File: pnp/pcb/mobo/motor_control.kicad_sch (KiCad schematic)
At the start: 0 parts

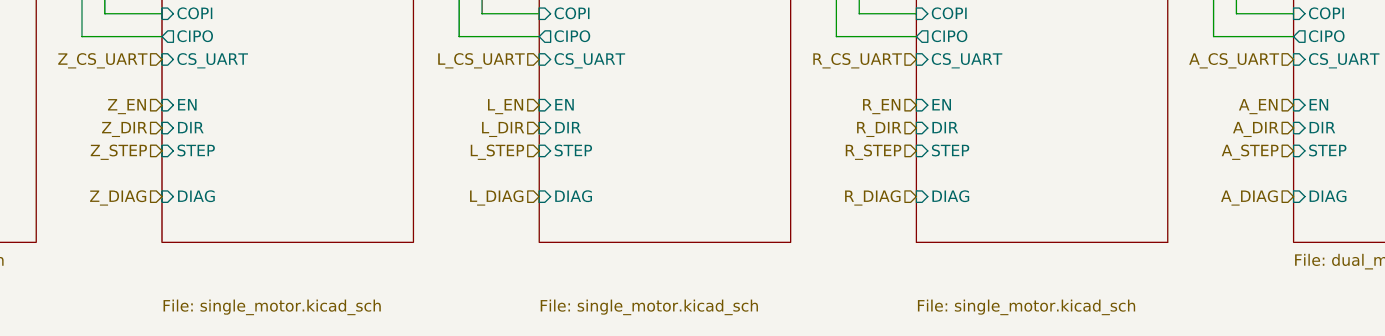
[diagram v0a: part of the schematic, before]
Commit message: Mobo V4A Redesign
Some EMC improvements to schematics.
Reassigned MCU Pins for HW-PWM support.
Changes are still marked with text in the schematics.
Complete PCB Layout reworked
Status: Needs to be verified, and cleaned up a little, but DRC is running green.
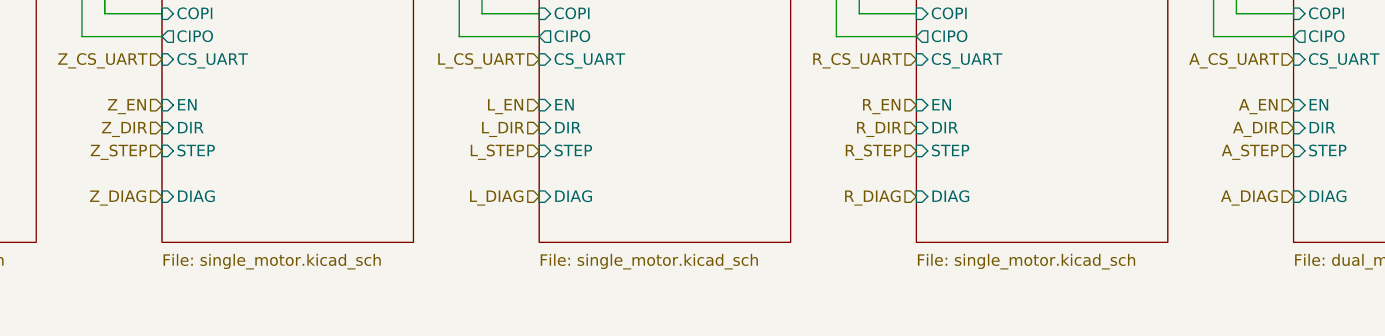
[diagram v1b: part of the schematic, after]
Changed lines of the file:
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@@
   (title_block
     (title "LumenPnP Motherboard")
-    (date "2022-03-29")
-    (rev "003")
+    (date "2022-09-09")
+    (rev "004A")
     (company "Opulo")
+    (comment 1 "Reengineered by Magpie")
   )
   (junction (at 114.3 81.28) (diameter 0) (color 0 0 0 0)
@@
       (effects (font (size 1.27 1.27)) (justify left bottom))
     )
-    (property "Sheet file" "single_motor.kicad_sch" (id 1) (at 78.74 127 0)
+    (property "Sheet file" "single_motor.kicad_sch" (id 1) (at 78.74 121.92 0)
       (effects (font (size 1.27 1.27)) (justify left top))
     )
@@
       (effects (font (size 1.27 1.27)) (justify left bottom))
     )
-    (property "Sheet file" "single_motor.kicad_sch" (id 1) (at 162.56 127 0)
+    (property "Sheet file" "single_motor.kicad_sch" (id 1) (at 162.56 121.92 0)
       (effects (font (size 1.27 1.27)) (justify left top))
     )
@@
       (effects (font (size 1.27 1.27)) (justify left bottom))
     )
-    (property "Sheet file" "single_motor.kicad_sch" (id 1) (at 120.65 127 0)
-      (effects (font (size 1.27 1.27)) (justify left top))
-    )
+    (property "Sheet file" "single_motor.kicad_sch" (id 1) (at 120.65 121.92 0)
+      (effects (font (size 1.27 1.27)) (justify left top))
+    )

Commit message: Redesign finished
Completed Board redesign and adding more EMC improvements.
Changed all the part numbers to have a Mouser orderable design (except the JST connectors)
All outputs generated
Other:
- company: Opulo -> Opulo.io
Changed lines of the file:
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@@
   (title_block
     (title "LumenPnP Motherboard")
-    (date "2022-09-09")
-    (rev "004A")
-    (company "Opulo")
+    (date "2022-10-06")
+    (rev "04A")
+    (company "Opulo.io")
     (comment 1 "Reengineered by Magpie")
   )
